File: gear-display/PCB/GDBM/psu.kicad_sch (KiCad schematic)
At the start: 13 parts, among them J3 DC_2.1_5.5_54-00286, U1 DC_DC_5V_2A0_GAPTEC_OKI-78SR-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

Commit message: layout
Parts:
- C1, C2, C3: value C_1206_10u_50V -> C_1206_10u_X5R_50V_automotive; symbol KD_Capacitor:C_1206_10u_50V -> KD_Capacitor:C_1206_10u_X5R_50V_automotive; Code 10 uF -> 10u; MFG_PartNo CL31B106KBHNNNE -> GRT31CR61H106ME01L; Manufacturer Samsung Electro-Mechanics -> Murata Electronics; Price 0.10 -> 0.30; Supplier_PartNo 1276-6767-1-ND -> 490-12457-1-ND
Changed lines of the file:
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@@
   (title_block
     (title "Gear Display Board")
-    (date "2022-08-13")
-    (rev "1.0")
+    (date "2023-01-05")
+    (rev "2.0")
     (company "Kallio Designs Oy")
     (comment 1 "Teemu Latonen")
@@
     (pin "3")
   )
-  (symbol (lib_id "KD_Capacitor:C_1206_10u_50V") (at 167.64 105.41 0) (unit 1)
+  (symbol (lib_id "KD_Capacitor:C_1206_10u_X5R_50V_automotive") (at 167.64 105.41 0) (unit 1)
     (in_bom yes) (on_board yes) (fields_autoplaced)
     (property "Reference" "C1" (id 0) (at 171.45 104.1399 0)
       (effects (font (size 1.27 1.27)) (justify left))
     )
-    (property "Value" "C_1206_10u_50V" (id 1) (at 154.94 73.66 0)
+    (property "Value" "C_1206_10u_X5R_50V_automotive" (id 1) (at 154.94 73.66 0)
       (effects (font (size 1.27 1.27)) (justify left) hide)
     )
@@
       (effects (font (size 1.27 1.27)) (justify left) hide)
     )
-    (property "Datasheet" "datasheet" (id 3) (at 154.94 93.98 0)
-      (effects (font (size 1.27 1.27)) (justify left) hide)
-    )
-    (property "Code" "10 uF" (id 4) (at 171.45 106.6799 0)
-      (effects (font (size 1.27 1.27)) (justify left))
-    )
-    (property "Manufacturer" "Samsung Electro-Mechanics" (id 5) (at 154.94 76.2 0)
-      (effects (font (size 1.27 1.27)) (justify left) hide)
-    )
-    (property "MFG_PartNo" "CL31B106KBHNNNE" (id 6) (at 154.94 78.74 0)
+    (property "Datasheet" "https://search.murata.co.jp/Ceramy/image/img/A01X/G101/ENG/GRT31CR61H106ME01-01.pdf" (id 3) (at 154.94 93.98 0)
+      (effects (font (size 1.27 1.27)) (justify left) hide)
+    )
+    (property "Code" "10u" (id 4) (at 171.45 106.6799 0)
+      (effects (font (size 1.27 1.27)) (justify left))
+    )
+    (property "Manufacturer" "Murata Electronics" (id 5) (at 154.94 76.2 0)
+      (effects (font (size 1.27 1.27)) (justify left) hide)
+    )
+    (property "MFG_PartNo" "GRT31CR61H106ME01L" (id 6) (at 154.94 78.74 0)
       (effects (font (size 1.27 1.27)) (justify left) hide)
     )
@@
       (effects (font (size 1.27 1.27)) (justify left) hide)
     )
-    (property "Supplier_PartNo" "1276-6767-1-ND" (id 8) (at 154.94 83.82 0)
+    (property "Supplier_PartNo" "490-12457-1-ND" (id 8) (at 154.94 83.82 0)
       (effects (font (size 1.27 1.27)) (justify left) hide)
     )
@@
       (effects (font (size 1.27 1.27)) (justify left) hide)
     )
-    (property "Price" "0.10" (id 10) (at 154.94 88.9 0)
+    (property "Price" "0.30" (id 10) (at 154.94 88.9 0)
       (effects (font (size 1.27 1.27)) (justify left) hide)
     )
@@
     (pin "1")
   )
-  (symbol (lib_id "KD_Capacitor:C_1206_10u_50V") (at 177.8 54.61 0) (unit 1)
+  (symbol (lib_id "KD_Capacitor:C_1206_10u_X5R_50V_automotive") (at 177.8 54.61 0) (unit 1)
     (in_bom yes) (on_board yes) (fields_autoplaced)
     (property "Reference" "C2" (id 0) (at 181.61 53.3399 0)
       (effects (font (size 1.27 1.27)) (justify left))
     )
-    (property "Value" "C_1206_10u_50V" (id 1) (at 165.1 22.86 0)
+    (property "Value" "C_1206_10u_X5R_50V_automotive" (id 1) (at 165.1 22.86 0)
       (effects (font (size 1.27 1.27)) (justify left) hide)
     )
@@
       (effects (font (size 1.27 1.27)) (justify left) hide)
     )
-    (property "Datasheet" "datasheet" (id 3) (at 165.1 43.18 0)
-      (effects (font (size 1.27 1.27)) (justify left) hide)
-    )
-    (property "Code" "10 uF" (id 4) (at 181.61 55.8799 0)
-      (effects (font (size 1.27 1.27)) (justify left))
-    )
-    (property "Manufacturer" "Samsung Electro-Mechanics" (id 5) (at 165.1 25.4 0)
-      (effects (font (size 1.27 1.27)) (justify left) hide)
-    )
-    (property "MFG_PartNo" "CL31B106KBHNNNE" (id 6) (at 165.1 27.94 0)
+    (property "Datasheet" "https://search.murata.co.jp/Ceramy/image/img/A01X/G101/ENG/GRT31CR61H106ME01-01.pdf" (id 3) (at 165.1 43.18 0)
+      (effects (font (size 1.27 1.27)) (justify left) hide)
+    )
+    (property "Code" "10u" (id 4) (at 181.61 55.8799 0)
+      (effects (font (size 1.27 1.27)) (justify left))
+    )
+    (property "Manufacturer" "Murata Electronics" (id 5) (at 165.1 25.4 0)
+      (effects (font (size 1.27 1.27)) (justify left) hide)
+    )
+    (property "MFG_PartNo" "GRT31CR61H106ME01L" (id 6) (at 165.1 27.94 0)
       (effects (font (size 1.27 1.27)) (justify left) hide)
     )
@@
       (effects (font (size 1.27 1.27)) (justify left) hide)
     )
-    (property "Supplier_PartNo" "1276-6767-1-ND" (id 8) (at 165.1 33.02 0)
+    (property "Supplier_PartNo" "490-12457-1-ND" (id 8) (at 165.1 33.02 0)
       (effects (font (size 1.27 1.27)) (justify left) hide)
     )
@@
       (effects (font (size 1.27 1.27)) (justify left) hide)
     )
-    (property "Price" "0.10" (id 10) (at 165.1 38.1 0)
+    (property "Price" "0.30" (id 10) (at 165.1 38.1 0)
       (effects (font (size 1.27 1.27)) (justify left) hide)
     )
@@
     (pin "2")
   )
-  (symbol (lib_id "KD_Capacitor:C_1206_10u_50V") (at 181.61 105.41 0) (unit 1)
+  (symbol (lib_id "KD_Capacitor:C_1206_10u_X5R_50V_automotive") (at 181.61 105.41 0) (unit 1)
     (in_bom yes) (on_board yes) (fields_autoplaced)
     (property "Reference" "C3" (id 0) (at 185.42 104.1399 0)
       (effects (font (size 1.27 1.27)) (justify left))
     )
-    (property "Value" "C_1206_10u_50V" (id 1) (at 168.91 73.66 0)
+    (property "Value" "C_1206_10u_X5R_50V_automotive" (id 1) (at 168.91 73.66 0)
       (effects (font (size 1.27 1.27)) (justify left) hide)
     )
@@
       (effects (font (size 1.27 1.27)) (justify left) hide)
     )
-    (property "Datasheet" "datasheet" (id 3) (at 168.91 93.98 0)
-      (effects (font (size 1.27 1.27)) (justify left) hide)
-    )
-    (property "Code" "10 uF" (id 4) (at 185.42 106.6799 0)
-      (effects (font (size 1.27 1.27)) (justify left))
-    )
-    (property "Manufacturer" "Samsung Electro-Mechanics" (id 5) (at 168.91 76.2 0)
-      (effects (font (size 1.27 1.27)) (justify left) hide)
-    )
-    (property "MFG_PartNo" "CL31B106KBHNNNE" (id 6) (at 168.91 78.74 0)
+    (property "Datasheet" "https://search.murata.co.jp/Ceramy/image/img/A01X/G101/ENG/GRT31CR61H106ME01-01.pdf" (id 3) (at 168.91 93.98 0)
+      (effects (font (size 1.27 1.27)) (justify left) hide)
+    )
+    (property "Code" "10u" (id 4) (at 185.42 106.6799 0)
+      (effects (font (size 1.27 1.27)) (justify left))
+    )
+    (property "Manufacturer" "Murata Electronics" (id 5) (at 168.91 76.2 0)
+      (effects (font (size 1.27 1.27)) (justify left) hide)
+    )
+    (property "MFG_PartNo" "GRT31CR61H106ME01L" (id 6) (at 168.91 78.74 0)
       (effects (font (size 1.27 1.27)) (justify left) hide)
     )
@@
       (effects (font (size 1.27 1.27)) (justify left) hide)
     )
-    (property "Supplier_PartNo" "1276-6767-1-ND" (id 8) (at 168.91 83.82 0)
+    (property "Supplier_PartNo" "490-12457-1-ND" (id 8) (at 168.91 83.82 0)
       (effects (font (size 1.27 1.27)) (justify left) hide)
     )
@@
       (effects (font (size 1.27 1.27)) (justify left) hide)
     )
-    (property "Price" "0.10" (id 10) (at 168.91 88.9 0)
-      (effects (font (size 1.27 1.27)) (justify left) hide)
-    )
+    (property "Price" "0.30" (id 10) (at 168.91 88.9 0)
+      (effects (font (size 1.27 1.27)) (justify left) hide)
+    )

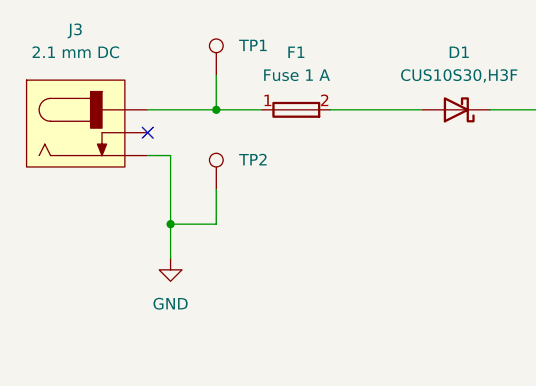
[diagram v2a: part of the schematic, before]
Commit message: change to kicad 7
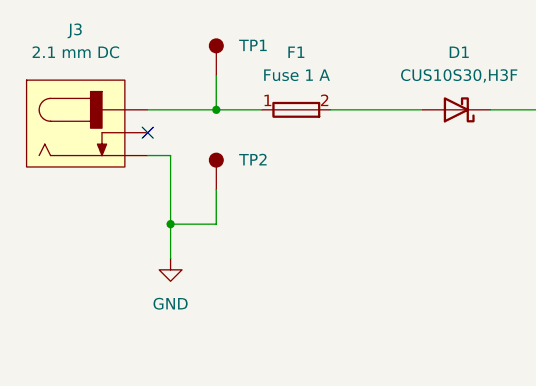
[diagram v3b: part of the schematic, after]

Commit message: version numbering fix
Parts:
- removed C22: C_0805_22u_X5R_10V, KD_Capacitor:CAPC2012X135N, symbol KD_Capacitor:C_0805_22u_X5R_10V
- added C22, C26: C_1206_10u_X5R_50V_automotive, KD_Capacitor:CAPC3216X150N, symbol KD_Capacitor:C_1206_10u_X5R_50V_automotive
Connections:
- net +12V: now also C22.1, C26.1
- net Earth: now also C22.2, C26.2
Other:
- moved on the sheet: C1, C3, C5

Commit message: Layout
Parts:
- C1, C2, C22, C26, C3: value C_1206_10u_X5R_50V_automotive -> 10u
- C4, C5: value C_0603_100n_X7R_100V -> 100n
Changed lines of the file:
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@@
       (effects (font (size 1.27 1.27)) (justify left))
     )
-    (property "Value" "C_0603_100n_X7R_100V" (at 182.88 22.86 0)
+    (property "Value" "100n" (at 182.88 22.86 0)
       (effects (font (size 1.27 1.27)) (justify left) hide)
     )
@@
       (effects (font (size 1.27 1.27)) (justify left))
     )
-    (property "Value" "C_1206_10u_X5R_50V_automotive" (at 151.13 71.12 0)
+    (property "Value" "10u" (at 151.13 71.12 0)
       (effects (font (size 1.27 1.27)) (justify left) hide)
     )
@@
       (effects (font (size 1.27 1.27)) (justify left))
     )
-    (property "Value" "C_1206_10u_X5R_50V_automotive" (at 165.1 22.86 0)
+    (property "Value" "10u" (at 165.1 22.86 0)
       (effects (font (size 1.27 1.27)) (justify left) hide)
     )
@@
       (effects (font (size 1.27 1.27)) (justify left))
     )
-    (property "Value" "C_1206_10u_X5R_50V_automotive" (at 105.41 71.12 0)
+    (property "Value" "10u" (at 105.41 71.12 0)
       (effects (font (size 1.27 1.27)) (justify left) hide)
     )
@@
       (effects (font (size 1.27 1.27)) (justify left))
     )
-    (property "Value" "C_0603_100n_X7R_100V" (at 179.07 71.12 0)
+    (property "Value" "100n" (at 179.07 71.12 0)
       (effects (font (size 1.27 1.27)) (justify left) hide)
     )
@@
       (effects (font (size 1.27 1.27)) (justify left))
     )
-    (property "Value" "C_1206_10u_X5R_50V_automotive" (at 165.1 71.12 0)
+    (property "Value" "10u" (at 165.1 71.12 0)
       (effects (font (size 1.27 1.27)) (justify left) hide)
     )
@@
       (effects (font (size 1.27 1.27)) (justify left))
     )
-    (property "Value" "C_1206_10u_X5R_50V_automotive" (at 119.38 71.12 0)
-      (effects (font (size 1.27 1.27)) (justify left) hide)
-    )
+    (property "Value" "10u" (at 119.38 71.12 0)
+      (effects (font (size 1.27 1.27)) (justify left) hide)
+    )
